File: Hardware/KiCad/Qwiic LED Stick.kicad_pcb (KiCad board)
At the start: 4 copper layers, 91.4 x 25.4 mm, 68 parts, among them J1 CONN_021X02_NO_SILK, J2 SMD, J3 PTH, J4 SMD, J5 CONN_041X04_NO_SILK, J6 AVR_SPI_PROG_3X2TESTPOINTS, U1 Tiny85-20-SMT

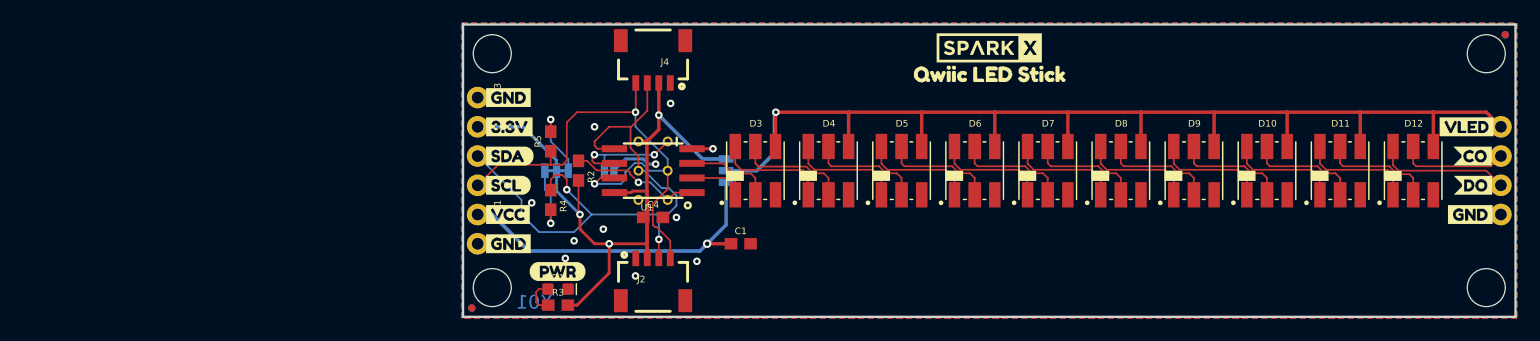
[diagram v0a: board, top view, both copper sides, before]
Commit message: created a smaller Board
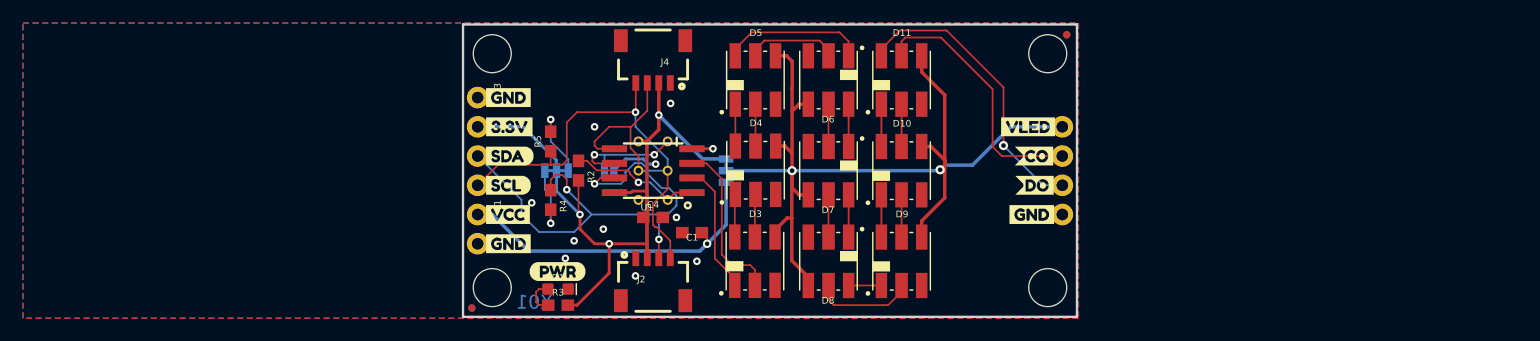
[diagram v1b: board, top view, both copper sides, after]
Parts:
- removed D12: APA1025050, Qwiic LED Stick:APA102-5050
- U$1, U$32: moved to B.Cu
- moved D11 38.9 mm to (140.9, 97.1)
- moved U$12 38.1 mm to (149.8, 108.8)
- moved U$29 38.1 mm to (149.4, 113.5)
- moved U$9 38.1 mm to (149.0, 101.2)
- moved J5 38.1 mm to (154.9, 101.2)
- moved JP2 38.1 mm to (155.2, 93.2)
- moved JP5 38.1 mm to (155.2, 93.2)
- moved JP7 38.1 mm to (153.6, 94.8)
- moved JP8 38.1 mm to (153.6, 115.2)
- moved U$15 38.1 mm to (150.7, 106.3)
- moved U$16 38.1 mm to (150.7, 103.7)
- moved U$5 38.1 mm to (154.7, 101.2)
- moved U$6 38.1 mm to (154.6, 106.3)
- moved U$7 38.1 mm to (154.6, 103.7)
- moved U$8 38.1 mm to (154.6, 108.8)
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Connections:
- D11 pad P5: Net-(D11-PadP5) -> /CO(10)
- D11 pad P6: Net-(D11-PadP6) -> /DO(10)
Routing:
- net /VLED: track 101.9 -> 83.0 mm, vias 1 -> 2
- net /DO(10): track 11.7 -> 25.5 mm, vias 0 -> 1
- net /CO(10): track 9.56 -> 22.6 mm
- net Net-(D11-PadP6): track 10.0 -> 0.00 mm
- net Net-(D11-PadP5): track 9.82 -> 0.00 mm
- net /CLK: track 7.50 -> 14.5 mm
- net Net-(D8-PadP6): track 9.81 -> 2.85 mm
- net Net-(D10-PadP1): track 10.4 -> 3.67 mm
- net Net-(D3-PadP6): track 9.95 -> 3.72 mm
- net /DO: track 5.14 -> 11.3 mm
- net Net-(D4-PadP6): track 9.81 -> 3.64 mm
- net Net-(D4-PadP5): track 9.81 -> 3.64 mm
- net Net-(D6-PadP5): track 9.81 -> 3.67 mm
- net Net-(D10-PadP5): track 9.81 -> 3.67 mm
- net Net-(D6-PadP6): track 9.81 -> 3.67 mm
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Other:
- board size 91.4 x 25.4 mm -> 53.3 x 25.4 mm

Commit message: Removed 2 inner layers
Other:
- copper layers 4 -> 2
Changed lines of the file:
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@@
   (layers
     (0 F.Cu signal)
-    (1 In1.Cu signal)
-    (2 In2.Cu signal)
     (31 B.Cu signal)
     (32 B.Adhes user)
@@
   )
   (setup
-    (last_trace_width 0.3048)
+    (last_trace_width 0.1524)
     (user_trace_width 0.1524)
     (user_trace_width 0.254)

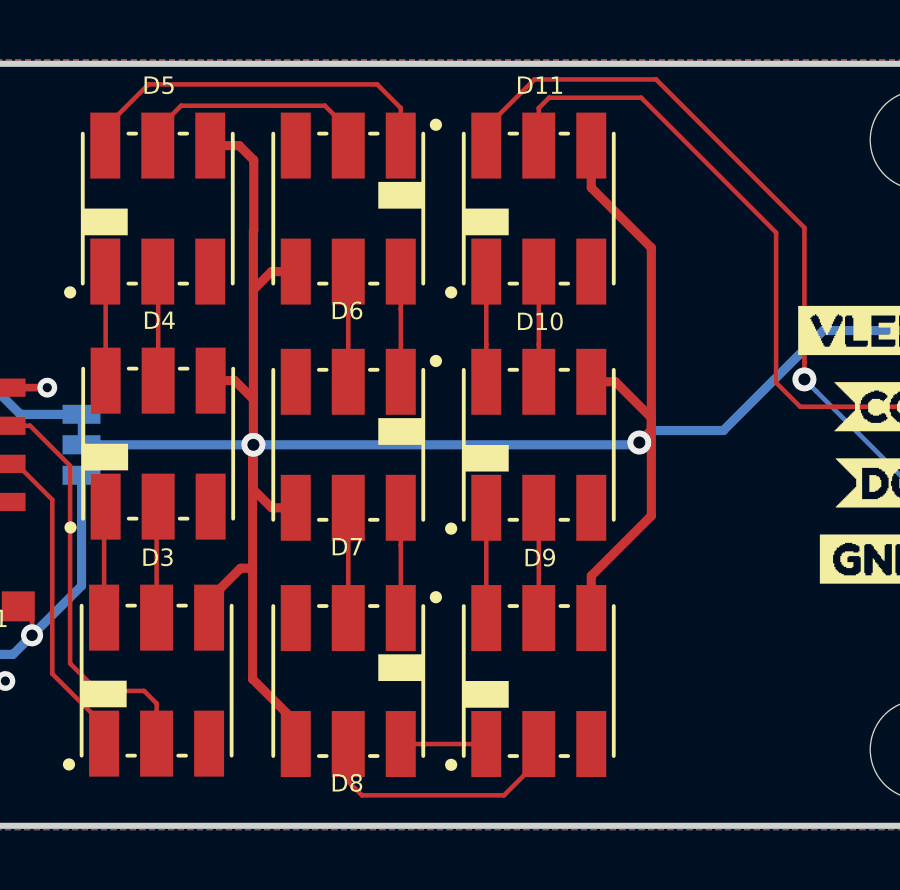
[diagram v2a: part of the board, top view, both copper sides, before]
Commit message: added a few Vias to the Ground Plane to reduce ground loops
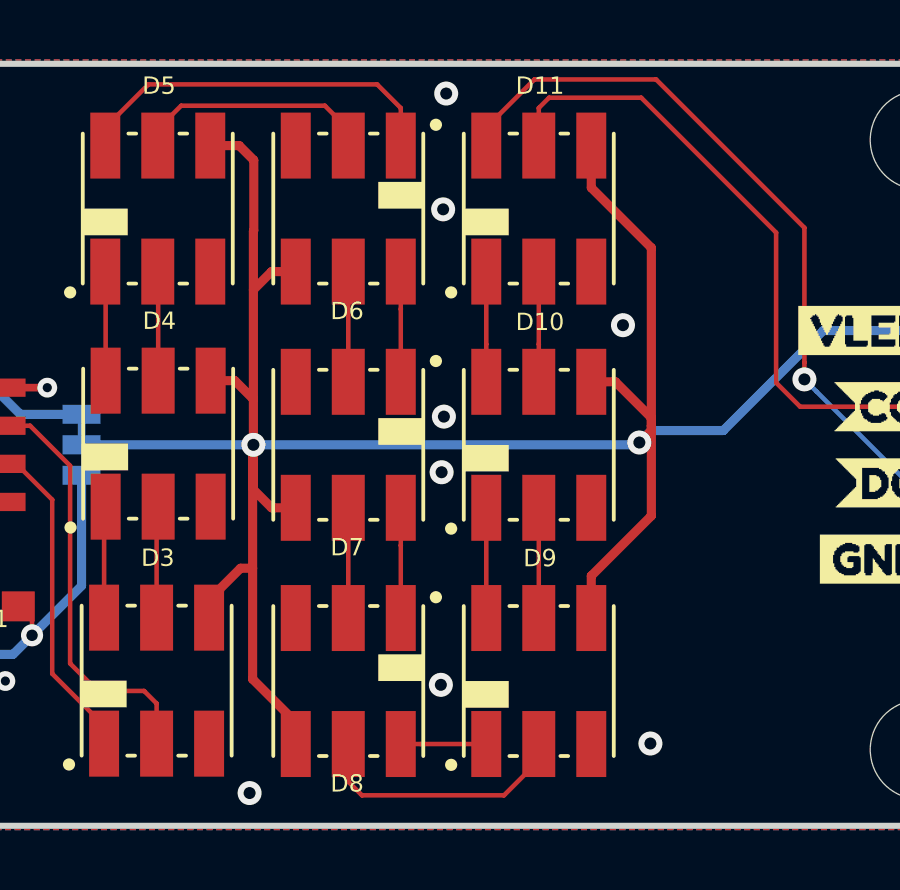
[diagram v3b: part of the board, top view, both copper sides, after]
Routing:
- net GND: vias 11 -> 19
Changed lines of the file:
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@@
     (thickness 1.6)
     (drawings 11)
-    (tracks 278)
+    (tracks 286)
     (zones 0)
     (modules 67)
@@
   (via (at 108.7501 107.7976) (size 0.6604) (drill 0.3048) (layers F.Cu B.Cu) (net 2))
   (via (at 123.1011 112.8776) (size 0.6604) (drill 0.3048) (layers F.Cu B.Cu) (net 2))
+  (via (at 137.6172 113.0046) (size 0.8) (drill 0.4) (layers F.Cu B.Cu) (net 2))
+  (via (at 137.6426 105.918) (size 0.8) (drill 0.4) (layers F.Cu B.Cu) (net 2))
+  (via (at 137.7188 104.0638) (size 0.8) (drill 0.4) (layers F.Cu B.Cu) (net 2))
+  (via (at 137.6934 97.155) (size 0.8) (drill 0.4) (layers F.Cu B.Cu) (net 2))
+  (via (at 137.795 93.2942) (size 0.8) (drill 0.4) (layers F.Cu B.Cu) (net 2))
+  (via (at 131.2418 116.6114) (size 0.8) (drill 0.4) (layers F.Cu B.Cu) (net 2))
+  (via (at 144.6022 114.9604) (size 0.8) (drill 0.4) (layers F.Cu B.Cu) (net 2))
+  (via (at 143.6878 101.0158) (size 0.8) (drill 0.4) (layers F.Cu B.Cu) (net 2))
   (segment (start 104.0511 108.8136) (end 105.3211 108.8136) (width 0.3048) (layer B.Cu) (net 3))
   (segment (start 108.4961 111.9886) (end 123.3551 111.9886) (width 0.3048) (layer B.Cu) (net 3))
